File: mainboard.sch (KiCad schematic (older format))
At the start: 48 parts, among them IC1 BMX160, J1 Conn_01x01, J2 10118194-0001LF, J28 Conn_01x01, J29 Conn_01x01, J3 Micro_SD_Card, J30 Conn_01x01, J4 xf2m-2415-1a, J5 XF2M-1015-1A, SW1 KMR231NG LFS, U1 RFM95W-915S2, U2 ATSAMD51G_TQFN48, U3 DRV8848, U4 TPS82740BSIPR, U5 DRV8848, U6 MAX708RESA-T, U8 RFM95W-915S2, X1 ANTENNA_U.FL, X2 ANTENNA_U.FL

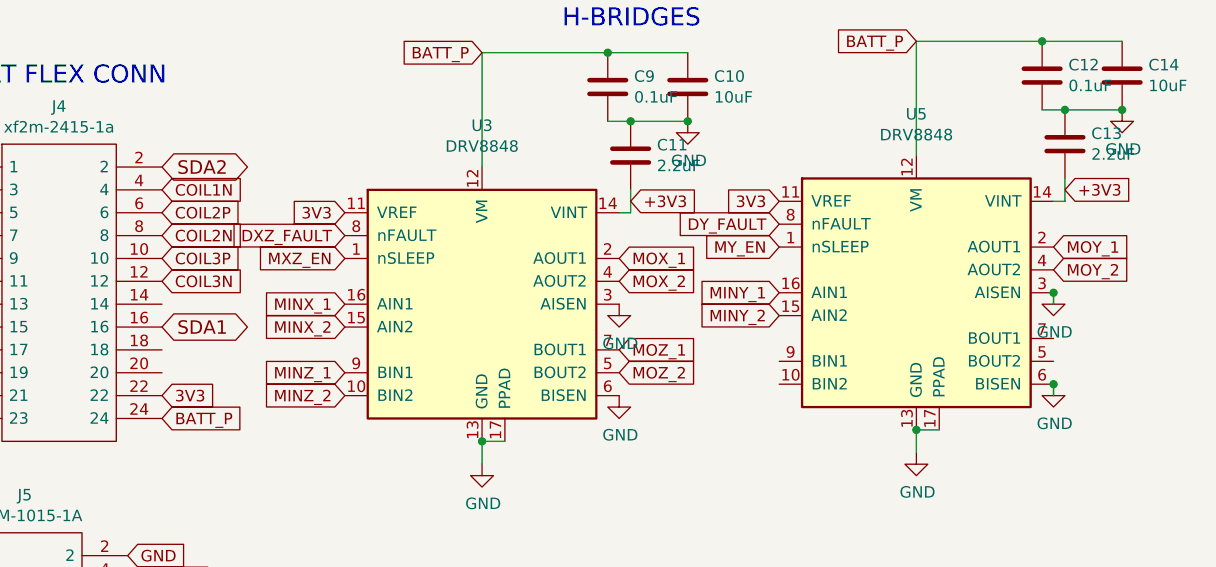
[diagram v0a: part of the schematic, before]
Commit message: added routing for flex connectors to hbridge
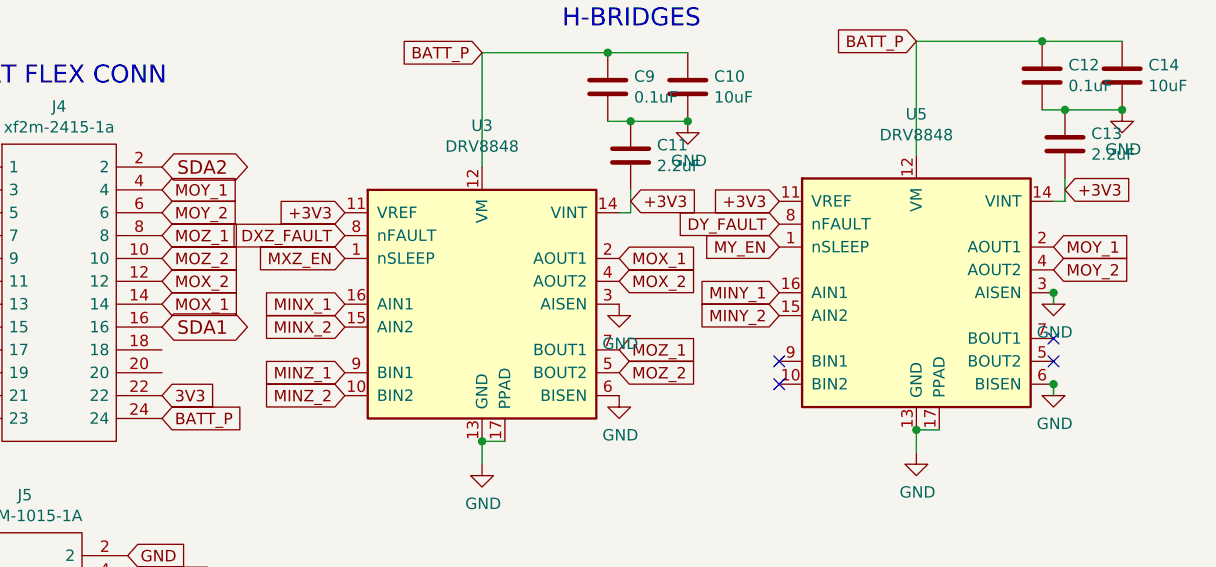
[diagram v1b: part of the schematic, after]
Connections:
- net labels removed: COIL1N, COIL2N, COIL2P, COIL3N, COIL3P
- no-connect marks 10 -> 14
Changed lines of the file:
@@
 COIL1P
 Text GLabel 6100 1350 2    50   Input ~ 0
-COIL1N
+MOY_1
 Wire Wire Line
 	4750 1450 4700 1450
@@
 	4750 1450 4750 1500
 Text GLabel 6100 1450 2    50   Input ~ 0
-COIL2P
+MOY_2
 Text GLabel 6100 1550 2    50   Input ~ 0
-COIL2N
-Text GLabel 6100 1650 2    50   Input ~ 0
-COIL3P
+MOZ_1
 Text GLabel 6100 1750 2    50   Input ~ 0
-COIL3N
+MOX_2
 Text GLabel 5300 5900 2    59   BiDi ~ 0
 SDA2
@@
 BATT_P
 Text GLabel 6900 1450 0    50   Input ~ 0
-3V3
++3V3
 Text GLabel 8150 1400 2    50   Input ~ 0
 +3V3
 Text GLabel 8800 1400 0    50   Input ~ 0
-3V3
++3V3
 Text GLabel 10050 1350 2    50   Input ~ 0
 +3V3
+Text GLabel 6100 1850 2    50   Input ~ 0
+MOX_1
+NoConn ~ 8800 2100
+NoConn ~ 8800 2200
+NoConn ~ 10000 2000
+NoConn ~ 10000 2100
+Text GLabel 6100 1650 2    50   Input ~ 0
+MOZ_2
 $EndSCHEMATC

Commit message: updated layout with new camera connector placement, more traces, removed mounting holes
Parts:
- removed H1, H2, H3, H4: MountingHole, MountingHole:MountingHole_2.2mm_M2, symbol Mechanical:MountingHole
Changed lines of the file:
@@
-$EndComp
-$Comp
-L Mechanical:MountingHole H4
-U 1 1 5DAAE797
-P 9850 6650
-F 0 "H4" H 9950 6696 50  0000 L CNN
-F 1 "MountingHole" H 9950 6605 50  0000 L CNN
-F 2 "MountingHole:MountingHole_2.2mm_M2" H 9850 6650 50  0001 C CNN
-F 3 "~" H 9850 6650 50  0001 C CNN
-	1    9850 6650
-	1    0    0    -1
-$EndComp
-$Comp
-L Mechanical:MountingHole H3
-U 1 1 5DAAFFA0
-P 9850 6450
-F 0 "H3" H 9950 6496 50  0000 L CNN
-F 1 "MountingHole" H 9950 6405 50  0000 L CNN
-F 2 "MountingHole:MountingHole_2.2mm_M2" H 9850 6450 50  0001 C CNN
-F 3 "~" H 9850 6450 50  0001 C CNN
-	1    9850 6450
-	1    0    0    -1
-$EndComp
-$Comp
-L Mechanical:MountingHole H1
-U 1 1 5DAB18C3
-P 8800 6450
-F 0 "H1" H 8700 6404 50  0000 R CNN
-F 1 "MountingHole" H 8700 6495 50  0000 R CNN
-F 2 "MountingHole:MountingHole_2.2mm_M2" H 8800 6450 50  0001 C CNN
-F 3 "~" H 8800 6450 50  0001 C CNN
-	1    8800 6450
-	-1   0    0    1
-$EndComp
-$Comp
-L Mechanical:MountingHole H2
-U 1 1 5DAB1C8C
-P 8800 6650
-F 0 "H2" H 8700 6604 50  0000 R CNN
-F 1 "MountingHole" H 8700 6695 50  0000 R CNN
-F 2 "MountingHole:MountingHole_2.2mm_M2" H 8800 6650 50  0001 C CNN
-F 3 "~" H 8800 6650 50  0001 C CNN
-	1    8800 6650
-	-1   0    0    1
 $EndComp
 $Comp

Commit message: updated footprints for U.FL connectors, more traces added
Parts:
- removed X2: ANTENNA_U.FL, Connector_Coaxial:U.FL_Molex_MCRF_73412-0110_Vertical, symbol mainboard-rescue:ANTENNA_U.FL-
- added X2: ANTENNA_U.FL, U.FL:UFL-R-SMT01, symbol mainboard-cache:mainboard-rescue_ANTENNA_U.FL-
- X1: footprint Connector_Coaxial:U.FL_Molex_MCRF_73412-0110_Vertical -> U.FL:UFL-R-SMT01
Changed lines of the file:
@@
-$EndComp
-$Comp
-L mainboard-rescue:ANTENNA_U.FL- X2
-U 1 1 5DAC9815
-P 10100 3900
-F 0 "X2" H 10150 3437 42  0000 C CNN
-F 1 "ANTENNA_U.FL" H 10150 3516 42  0000 C CNN
-F 2 "Connector_Coaxial:U.FL_Molex_MCRF_73412-0110_Vertical" H 10100 3900 50  0001 C CNN
-F 3 "" H 10100 3900 50  0001 C CNN
-	1    10100 3900
-	-1   0    0    1
 $EndComp
 $Comp
@@
 F 0 "X1" H 9150 4787 42  0000 C CNN
 F 1 "ANTENNA_U.FL" H 9150 4866 42  0000 C CNN
-F 2 "Connector_Coaxial:U.FL_Molex_MCRF_73412-0110_Vertical" H 9100 5250 50  0001 C CNN
+F 2 "U.FL:UFL-R-SMT01" H 9100 5250 50  0001 C CNN
 F 3 "" H 9100 5250 50  0001 C CNN
 	1    9100 5250
 	-1   0    0    1
 $EndComp
-$Comp
-L power:GND #PWR01
-U 1 1 5DACFA75
-P 10350 3750
-F 0 "#PWR01" H 10350 3500 50  0001 C CNN
-F 1 "GND" H 10355 3577 50  0000 C CNN
-F 2 "" H 10350 3750 50  0001 C CNN
-F 3 "" H 10350 3750 50  0001 C CNN
-	1    10350 3750
-	1    0    0    -1
-$EndComp
-Wire Wire Line
-	10350 3750 10200 3750
-Wire Wire Line
-	10200 3750 10200 3700
-Connection ~ 10200 3700
-Wire Wire Line
-	10200 3700 10200 3600
 Wire Wire Line
 	8900 5250 8900 5150
@@
 Text GLabel 6100 1650 2    50   Input ~ 0
 MOZ_2
+$Comp
+L mainboard-cache:mainboard-rescue_ANTENNA_U.FL- X2
+U 1 1 5DF0AD82
+P 10100 3900
+F 0 "X2" H 10150 3437 42  0000 C CNN
+F 1 "ANTENNA_U.FL" H 10150 3516 42  0000 C CNN
+F 2 "U.FL:UFL-R-SMT01" H 10100 3900 50  0001 C CNN
+F 3 "" H 10100 3900 50  0001 C CNN
+	1    10100 3900
+	-1   0    0    1
+$EndComp
+Wire Wire Line
+	10200 3600 10200 3700
+$Comp
+L power:GND #PWR0136
+U 1 1 5DF14AF0
+P 10250 3750
+F 0 "#PWR0136" H 10250 3500 50  0001 C CNN
+F 1 "GND" H 10255 3577 50  0000 C CNN
+F 2 "" H 10250 3750 50  0001 C CNN
+F 3 "" H 10250 3750 50  0001 C CNN
+	1    10250 3750
+	0    -1   -1   0
+$EndComp
+Wire Wire Line
+	10200 3700 10200 3750
+Wire Wire Line
+	10200 3750 10250 3750
+Connection ~ 10200 3700
 $EndSCHEMATC

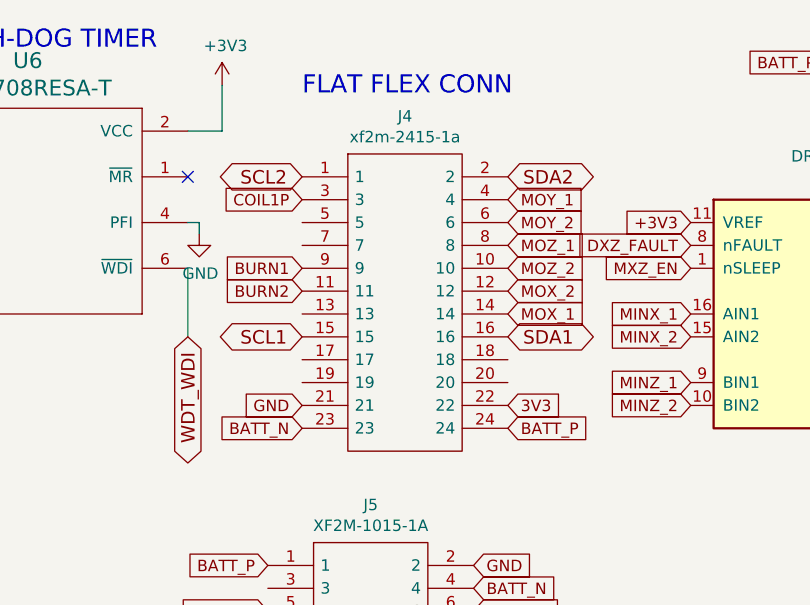
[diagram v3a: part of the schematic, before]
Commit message: adjusted ordering in flat flex connector to avoid ratsnest crossings for Hbridges, added camera traces
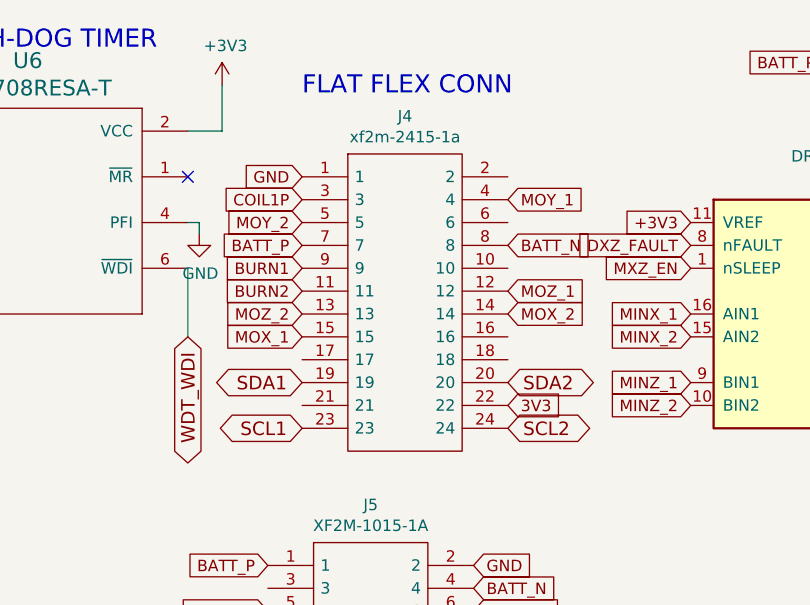
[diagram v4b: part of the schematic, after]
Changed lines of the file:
@@
 Text GLabel 6100 2250 2    50   Input ~ 0
 3V3
-Text GLabel 5200 2250 0    50   Input ~ 0
+Text GLabel 5200 1250 0    50   Input ~ 0
 GND
-Text GLabel 6100 2350 2    50   Input ~ 0
+Text GLabel 5200 1550 0    50   Input ~ 0
 BATT_P
-Text GLabel 5200 2350 0    50   Input ~ 0
+Text GLabel 6100 1550 2    50   Input ~ 0
 BATT_N
 Text GLabel 5200 1650 0    50   Input ~ 0
@@
 Wire Wire Line
 	4750 1450 4750 1500
-Text GLabel 6100 1450 2    50   Input ~ 0
+Text GLabel 5200 1450 0    50   Input ~ 0
 MOY_2
-Text GLabel 6100 1550 2    50   Input ~ 0
+Text GLabel 6100 1750 2    50   Input ~ 0
 MOZ_1
-Text GLabel 6100 1750 2    50   Input ~ 0
+Text GLabel 6100 1850 2    50   Input ~ 0
 MOX_2
 Text GLabel 5300 5900 2    59   BiDi ~ 0
@@
 Text Notes 2600 7900 0    50   ~ 0
 I2C_1\nSCL: PA01\nSDA: PA00\n\nI2C_2\nSCL: PA16\nSDA: PA17\n
-Text GLabel 6100 1950 2    59   BiDi ~ 0
+Text GLabel 5200 2150 0    59   BiDi ~ 0
 SDA1
-Text GLabel 5200 1950 0    59   BiDi ~ 0
+Text GLabel 5200 2350 0    59   BiDi ~ 0
 SCL1
-Text GLabel 5200 1250 0    59   BiDi ~ 0
+Text GLabel 6100 2350 2    59   BiDi ~ 0
 SCL2
-Text GLabel 6100 1250 2    59   BiDi ~ 0
+Text GLabel 6100 2150 2    59   BiDi ~ 0
 SDA2
 Wire Wire Line
@@
 Text GLabel 10050 1350 2    50   Input ~ 0
 +3V3
-Text GLabel 6100 1850 2    50   Input ~ 0
+Text GLabel 5200 1950 0    50   Input ~ 0
 MOX_1
 NoConn ~ 8800 2100
@@
 NoConn ~ 10000 2000
 NoConn ~ 10000 2100
-Text GLabel 6100 1650 2    50   Input ~ 0
+Text GLabel 5200 1850 0    50   Input ~ 0
 MOZ_2
 $Comp

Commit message: adding v01 + repo overhaul
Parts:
- removed D1: GREEN, LED_SMD:LED_0603_1608Metric, symbol mainboard-rescue:LED0805_NOOUTLINE-
- removed J1, J28, J29, J30: Conn_01x01, custom-footprints:castellated_small_1side, symbol mainboard-rescue:Conn_01x01-Connector_Generic
- removed X1: ANTENNA_U.FL, U.FL:UFL-R-SMT01, symbol mainboard-rescue:ANTENNA_U.FL-
- removed X2: ANTENNA_U.FL, U.FL:UFL-R-SMT01, symbol mainboard-cache:mainboard-rescue_ANTENNA_U.FL-
- added C15, C16, C17: 0.1uF, Capacitor_SMD:C_0402_1005Metric, symbol mainboard-rescue:C_Small-Device
- added C18: 1uF, Capacitor_SMD:C_0402_1005Metric, symbol mainboard-rescue:C_Small-Device
- added C19, C20: 22uF, Capacitor_SMD:C_0603_1608Metric, symbol mainboard-rescue:C-Device
- added D1, D4: D_Schottky, custom-footprints:MICROSMP, symbol Device:D_Schottky
- added D3: WS2812B, LED_SMD:LED_WS2812B_PLCC4_5.0x5.0mm_P3.2mm, symbol LED:WS2812B
- added FID1, FID2, FID3: Fiducial, Fiducial:Fiducial_0.5mm_Mask1mm, symbol Mechanical:Fiducial
- added J1: Conn_01x06, Connector_PinHeader_1.27mm:PinHeader_2x03_P1.27mm_Vertical_SMD, symbol Connector_Generic:Conn_01x06
- added J6, J7: U.FL-R-SMT-1, custom-footprints:U.FL-R-SMT-1, symbol symbols:U.FL-R-SMT-1
- added J9: Conn_01x02, Connector_PinHeader_2.54mm:PinHeader_1x02_P2.54mm_Vertical, symbol Connector_Generic:Conn_01x02
- added Q1: RADFET, Package_TO_SOT_SMD:SOT-23-6, symbol symbols:RADFET
- added R10, R13, R9: 100K, Resistor_SMD:R_0402_1005Metric, symbol mainboard-rescue:R_US-Device
- added R11, R12, R18, R19, R20, R21: 0, Resistor_SMD:R_0402_1005Metric, symbol mainboard-rescue:R_US-Device
- added R14, R15, R16, R17, R22, R23: 10K, Resistor_SMD:R_0402_1005Metric, symbol mainboard-rescue:R_US-Device
- added TP1, TP2: TestPoint, TestPoint:TestPoint_Keystone_5015_Micro-Minature, symbol Connector:TestPoint
- added U9: ADS124S06IRHBR, custom-footprints:ADS124208_withpad, symbol symbols:ADS124S06IRHBR
- J3: symbol Connector:Micro_SD_Card -> mainboard-rescue:Micro_SD_Card-Connector
- R1: value 330 -> 0
- renumbered IC1 to U7
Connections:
- net labels added: ADC_CS, BATTERY, COIL1_P, COIL2_N, COIL3_P, COIL4_N, COIL5_P, COIL6_N, M_EN, M_FAULT, M_FAULT2, RF1_BUSY, RF1_CS, RF1_IO1, RF1_RST, RF2_CS, RF2_IO1, ~DRDY
- net labels removed: 3V3, BATT_N, COIL1P, CS_IMU, CS_RF1, CS_RF2, DAC0, DAC1, DXZ_FAULT, DY_FAULT, LED1, MXZ_EN, MY_EN, PA04, PA07, PA21, PA22, PA23, RF_BUSY, RF_CS, RF_DIO0, RF_DIO1, RF_DIO2, RF_DIO3, RF_RST, RX, TX
- wire segments 169 -> 219
- no-connect marks 14 -> 12
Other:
- note added: "BATTERY CONN"
- note added: "CAMERA CONN"
- note added: "COIL1_N"
- note added: "COIL2_P"
- note added: "COIL3_N"
- note added: "COIL4_P"
- note added: "COIL5_N"
- note added: "COIL6_P"
- note added: "DOSIMETER"
- note added: "REGULATOR"
- note added: "SD CARD"
- note added: "X"
- note added: "Y"
- note added: "Z"
- note added: "current limit\nresistors"
- note added: "mainboard v01"
- note removed: "Regulator\n"
- note removed: "Sprite LoRa Generic"
- moved on the sheet: C1, C10, C11, C12, C13, C14, C2, C3, C4, C5, C6, C7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

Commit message: Updated magnetorquer driver and fixed some PCB DRC issues
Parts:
- removed C10, C14: 10uF, Capacitor_SMD:C_0402_1005Metric, symbol mainboard-rescue:C-Device
- removed C11, C13: 2.2uF, Capacitor_SMD:C_0402_1005Metric, symbol mainboard-rescue:C-Device
- removed C12, C9: 0.1uF, Capacitor_SMD:C_0402_1005Metric, symbol mainboard-rescue:C-Device
- removed C19, C20: 22uF, Capacitor_SMD:C_0603_1608Metric, symbol mainboard-rescue:C-Device
- removed D1, D4: D_Schottky, custom-footprints:MICROSMP, symbol Device:D_Schottky
- removed R18, R19: 0, Resistor_SMD:R_0402_1005Metric, symbol mainboard-rescue:R_US-Device
- removed U3, U5: DRV8848, KiCAD Libraries:SOP65P640X120-17N, symbol mainboard-rescue:DRV8848-Driver_Motor
- added C11, C12, C13, C20: 0.1uF, Capacitor_SMD:C_0402_1005Metric, symbol mainboard-rescue:C_Small-Device
- added C14: 10n, Capacitor_SMD:C_0402_1005Metric, symbol mainboard-rescue:C_Small-Device
- added C19: 10uF, Capacitor_SMD:C_0805_2012Metric, symbol mainboard-rescue:C_Small-Device
- added FL1, FL2, FL3: EMI_Filter_CommonMode, wbraun_smd:SRF2012, symbol Device:EMI_Filter_CommonMode
- added R24: 10k, Resistor_SMD:R_0402_1005Metric, symbol mainboard-rescue:R_US-Device
- added R25: 0, Resistor_SMD:R_0402_1005Metric, symbol mainboard-rescue:R_US-Device
- added U10: TPS22918-Q1, Package_TO_SOT_SMD:SOT-23-6, symbol wbraun_ic_lib:TPS22918-Q1
- added U11, U3, U5: DRV8830DRC, wbraun_smd:VSON-10, symbol wbraun_ic_lib:DRV8830DRC
- J6, J7: symbol symbols:U.FL-R-SMT-1 -> mainboard-rescue:U.FL-R-SMT-1-symbols
- Q1: symbol symbols:RADFET -> mainboard-rescue:RADFET-symbols
- R13: value 100K -> 10K
- U9: symbol symbols:ADS124S06IRHBR -> mainboard-rescue:ADS124S06IRHBR-symbols
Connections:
- net labels added: M_VCC, SCL3, SDA3
- net labels removed: MINX_1, MINX_2, MINY_1, MINY_2, MINZ_1, MINZ_2, M_FAULT2
- wire segments 219 -> 270
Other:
- note removed: "H-BRIDGES"
- note removed: "current limit\nresistors"
- moved on the sheet: C17, C18, C4, C8, D2, FID1, FID2, FID3, J3, J5, R15, R22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

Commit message: schematic work
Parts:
- removed C2: 10uF, Capacitor_SMD:C_0402_1005Metric, symbol mainboard-rescue:C_Small-Device
- removed C5: 1uF, Capacitor_SMD:C_0402_1005Metric, symbol mainboard-rescue:C_Small-Device
- removed J6, J7: U.FL-R-SMT-1, custom-footprints:U.FL-R-SMT-1, symbol mainboard-rescue:U.FL-R-SMT-1-symbols
- removed L1: 10uH, Inductor_SMD:L_0805_2012Metric, symbol mainboard-rescue:L_Small-Device
- removed R16, R17: 10K, Resistor_SMD:R_0402_1005Metric, symbol mainboard-rescue:R_US-Device
- removed U1, U8: RFM95W-915S2, RF_Module:HOPERF_RFM9XW_SMD, symbol mainboard-rescue:RFM95W-915S2-RF_AM_FM
- removed U2: ATSAMD51G_TQFN48, ATSAMD51G19A-MU:QFN50P700X700X90-49N-D, symbol mainboard-rescue:ATSAMD51G_TQFN48-
- added C?: 10uF, Capacitor_SMD:C_0402_1005Metric, symbol mainboard-rescue:C_Small-Device
- added C?: 1uF, Capacitor_SMD:C_0402_1005Metric, symbol mainboard-rescue:C_Small-Device
- added C? (x2): 0.1uF, Capacitor_SMD:C_0402_1005Metric, symbol mainboard-rescue:C_Small-Device
- added J?: U.FL-R-SMT-1, custom-footprints:U.FL-R-SMT-1, symbol mainboard-rescue:U.FL-R-SMT-1-symbols
- added L?: 10uH, Inductor_SMD:L_0805_2012Metric, symbol mainboard-rescue:L_Small-Device
- added R? (x2): 10K, Resistor_SMD:R_0402_1005Metric, symbol mainboard-rescue:R_US-Device
- added U?: RFM98PW-symbols, custom-footprints:RFM95PW, symbol mainboard-rescue:RFM98PW-symbols
- added U?: ATSAMD51J20A-M, Package_DFN_QFN:QFN-64-1EP_9x9mm_P0.5mm_EP4.7x4.7mm, symbol MCU_Microchip_SAMD:ATSAMD51J20A-M
- U10: symbol wbraun_ic_lib:TPS22918-Q1 -> mainboard-rescue:TPS22918-Q1-wbraun_ic_lib
- U11, U3, U5: symbol wbraun_ic_lib:DRV8830DRC -> mainboard-rescue:DRV8830DRC-wbraun_ic_lib
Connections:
- net +3V3: now also R5.2, C?.1, R?.2, U?.21 (VDDIOB), U?.34 (VDDIO), U?.48 (VDDIO), U?.56 (VDDIO), U?.8 (VDDANA), U?.9 (3.3V); no longer R5.1
- net ADC_CS: now also U?.40 (PB17)
- net BATTERY: now also C?.1, U?.15 (PA06)
- net BATT_P: now also U?.5 (VCC)
- net BURN1: now also U?.59 (PB30)
- net BURN2: now also U?.60 (PB31)
- net CS_CAM: now also U?.28 (PB15)
- net CS_SD: now also U?.51 (PA27)
- net EN_CAM: now also U?.39 (PB16)
- net GND: now also C?.2, C?.2, C?.2, C?.2, J?.1 (GND), J?.2, R?.1, U?.16 (GND), U?.17 (GND), U?.2 (GND), U?.22 (GND), U?.33 (GND), U?.47 (GND), U?.54 (GND), U?.65 (GND), U?.7 (GNDANA)
- net MISO: now also U?.10 (MISO), U?.31 (PA14)
- net MOSI: now also U?.11 (MOSI), U?.29 (PA12)
- net RF2_CS: now also R?.1, U?.13 (NSS)
- net SCK: now also U?.12 (SCK), U?.30 (PA13)
- net SCL1: now also U?.26 (PB13)
- net SCL2: now also R7.1, U?.35 (PA16); no longer R8.1
- net SDA1: now also U?.25 (PB12)
- net SDA2: now also R8.1, U?.36 (PA17); no longer R7.1
- net SWCLK: now also R5.1, U?.57 (PA30); no longer R5.2
- net SWDIO: now also U?.58 (PA31)
- net WDT_WDI: now also R?.2, U?.44 (PA23)
- net ~RESET: now also U?.52 (~RESET)
- net at D3.4 (DIN): now also U?.42 (PA21)
- net USB+ renamed USB_D+
- net USB_D+: now also U?.46 (PA25)
- net USB- renamed USB_D-
- net USB_D-: now also U?.45 (PA24)
- new net: J?.3 (ANT), U?.1 (ANT)
- new net: C?.1, C?.1, L?.2, U?.53 (VDDCORE)
- new net: L?.1, U?.55 (VSW)
- new net RF_BUSY: U?.14 (PA05), U?.4 (GPIO_4)
- new net RF_CS: U?.12 (PB09)
- new net RF_IO1: U?.13 (PA04), U?.7 (GPIO_1)
- new net RF_IO2: U?.8 (GPIO_2)
- new net RF_RST: U?.14 (RESET), U?.27 (PB14)
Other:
- note removed: "I2C_1\nSCL: PA01\nSDA: PA00\n\nI2C_2\nSCL: PA16\nSDA: PA17\n"
- note removed: "LoRa RADIO\n"
- moved on the sheet: C1, C15, C3, C6, C7, D3, J1, J2, R10, R2, R4, R5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

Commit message: finished schematic changes
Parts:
- removed J3: Micro_SD_Card, custom-footprints:503182-1853_MOLEX-MicroSD, symbol mainboard-rescue:Micro_SD_Card-Connector
- removed R15: 10K, Resistor_SMD:R_0402_1005Metric, symbol mainboard-rescue:R_US-Device
- added R? (x2): 10K, Resistor_SMD:R_0402_1005Metric, symbol mainboard-rescue:R_US-Device
- added U?: MR25H40, symbol Memory_NVRAM:MR25H40
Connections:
- net +3V3: now also R?.2, R?.2, U?.8 (VDD)
- net BURN1: now also U?.49 (PB22); no longer U?.59 (PB30)
- net BURN2: now also U?.50 (PB23); no longer U?.60 (PB31)
- net GND: now also U?.4 (VSS), U?.9 (PAD)
- net M_EN: now also U?.61 (PB00)
- net M_FAULT: now also U?.62 (PB01)
- net SCL3: now also U?.59 (PB30), R?.1
- net SDA3: now also U?.60 (PB31), R?.1
- net FLASH_MOSI: now reaches U?.17 (PA08)
- net FLASH_MOSI: now also U?.5 (SI)
- net FLASH_MISO: now reaches U?.18 (PA09)
- net FLASH_MISO: now also U?.2 (SO)
- net FLASH_IO2: now reaches U?.19 (PA10)
- net FLASH_IO2: now also U?.3 (~WP)
- net FLASH_IO3: now reaches U?.20 (PA11)
- net FLASH_IO3: now also U?.7 (~HOLD)
- net FLASH_SCK: now reaches U?.23 (PB10)
- net FLASH_SCK: now also U?.6 (SCK)
- net FLASH_CS: now reaches U?.24 (PB11)
- net FLASH_CS: now also U?.1 (~CS)
- net CS_SD: no longer names the net of U?.51 (PA27)
- no-connect marks 12 -> 10
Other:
- note added: "SERCOM0/2"
- note added: "SERCOM1"
- note added: "SERCOM4\n"
- note added: "SERCOM7"
- note removed: "SD CARD"
- note removed: "SPI\nSCK: PA09\nMOSI: PA08\nMISO: PA10\n"
- note removed: "UART:\nTX: PB08\nRX: PB09\n"
- moved on the sheet: R13, R14, R4, R6
